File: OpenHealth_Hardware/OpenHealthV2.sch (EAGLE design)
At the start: 21 parts

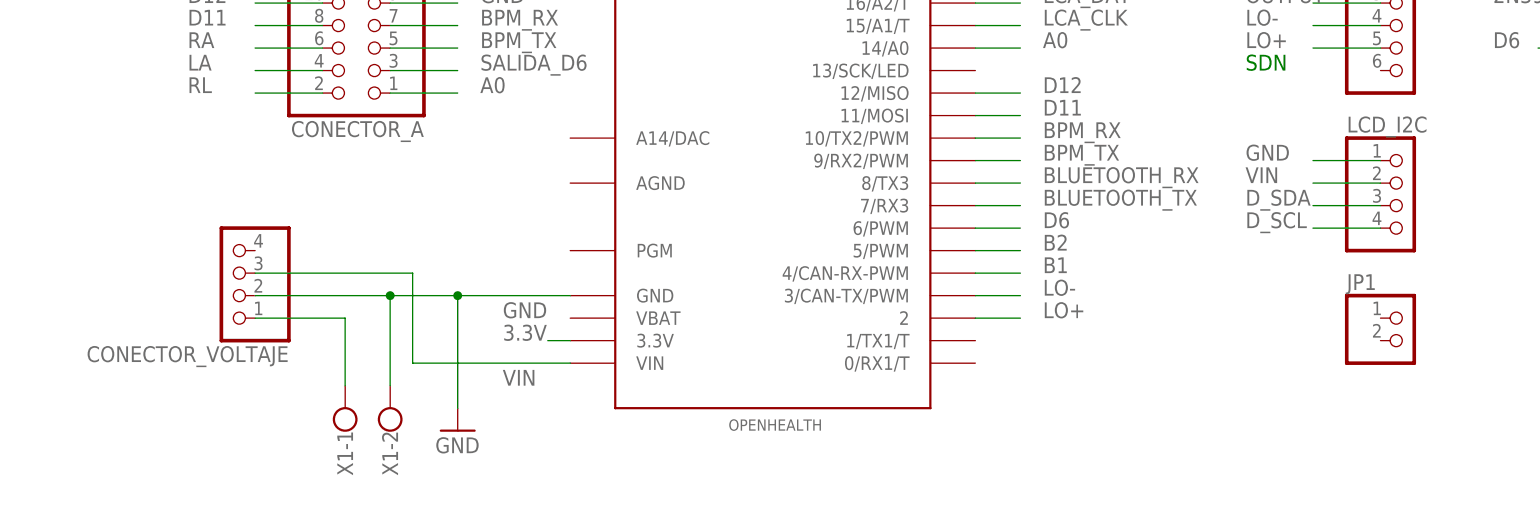
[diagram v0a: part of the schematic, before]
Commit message: Creacion de la Primera Libreria
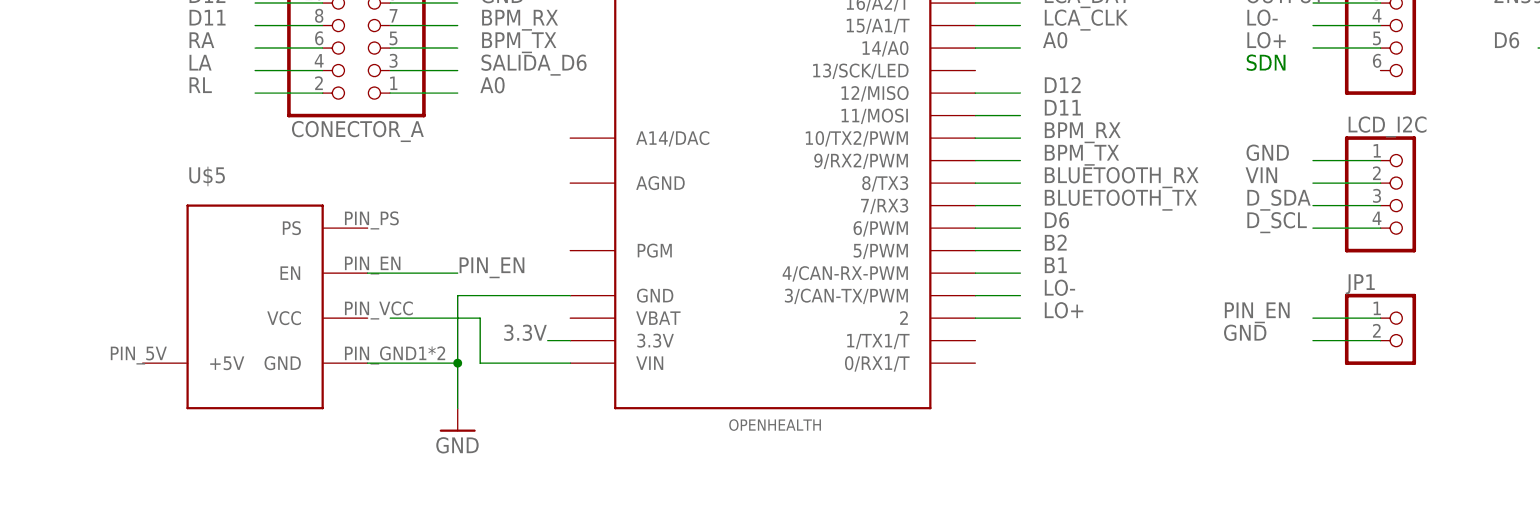
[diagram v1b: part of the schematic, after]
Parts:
- removed CONECTOR_VOLTAJE: (no value), pinhead:PINHD-1X4
- removed X1: (no value), con-wago-500:W237-102
- added U$5: LIPOWER, Bateria:LIPOWER
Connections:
- removed net N$1: CONECTOR_VOLTAJE.1, X1-1.KL
- new net N$5: OPENHEALTH.VIN
- new net PIN_EN: JP1.1, U$5.EN
- net GND: now also JP1.2, U$5.GND; no longer CONECTOR_VOLTAJE.2, X1-2.KL
- net VIN: no longer CONECTOR_VOLTAJE.3, OPENHEALTH.VIN
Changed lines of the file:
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@@
 <?xml version="1.0" encoding="utf-8"?>
 <!DOCTYPE eagle SYSTEM "eagle.dtd">
-<eagle version="7.2.0">
+<eagle version="7.7.0">
 <drawing>
 <settings>
@@
 <parts>
 <part name="OPENHEALTH" library="Teensy_3_and_LC_Series_Boards_v1.1" deviceset="TEENSY_3.1_OUTER_ROW" device=""/>
-<part name="CONECTOR_VOLTAJE" library="pinhead" deviceset="PINHD-1X4" device=""/>
-<part name="X1" library="con-wago-500" deviceset="W237-102" device=""/>
 <part name="CONECTOR_A" library="pinhead" deviceset="PINHD-2X5" device=""/>
 <part name="CONECTOR_B" library="pinhead" deviceset="PINHD-2X5" device=""/>
@@
 <part name="R4" library="resistor" deviceset="R-US_" device="0204/7" value="330"/>
 <part name="R5" library="resistor" deviceset="R-US_" device="0204/7" value="330"/>
+<part name="U$5" library="Bateria" deviceset="LIPOWER" device=""/>
 </parts>
 <sheets>
@@
 <instances>
 <instance part="OPENHEALTH" gate="G$1" x="-33.02" y="93.98" rot="R180"/>
-<instance part="CONECTOR_VOLTAJE" gate="A" x="-93.98" y="76.2" rot="R180"/>
-<instance part="X1" gate="-1" x="-81.28" y="58.42" rot="R90"/>
-<instance part="X1" gate="-2" x="-76.2" y="58.42" rot="R90"/>
 <instance part="CONECTOR_A" gate="A" x="-78.74" y="101.6" rot="R180"/>
 <instance part="CONECTOR_B" gate="A" x="-78.74" y="121.92" rot="R180"/>
@@
 <instance part="R4" gate="G$1" x="58.42" y="152.4" rot="R90"/>
 <instance part="R5" gate="G$1" x="66.04" y="152.4" rot="R90"/>
+<instance part="U$5" gate="G$1" x="-99.06" y="60.96"/>
 </instances>
 <busses>
 </busses>
 <nets>
-<net name="N$1" class="0">
-<segment>
-<pinref part="X1" gate="-1" pin="KL"/>
-<wire x1="-81.28" y1="71.12" x2="-81.28" y2="63.5" width="0.1524" layer="91"/>
-<pinref part="CONECTOR_VOLTAJE" gate="A" pin="1"/>
-<wire x1="-91.44" y1="71.12" x2="-81.28" y2="71.12" width="0.1524" layer="91"/>
-</segment>
-</net>
 <net name="GND" class="0">
-<segment>
-<pinref part="CONECTOR_VOLTAJE" gate="A" pin="2"/>
-<wire x1="-91.44" y1="73.66" x2="-76.2" y2="73.66" width="0.1524" layer="91"/>
-<pinref part="X1" gate="-2" pin="KL"/>
-<wire x1="-76.2" y1="73.66" x2="-68.58" y2="73.66" width="0.1524" layer="91"/>
-<wire x1="-68.58" y1="73.66" x2="-55.88" y2="73.66" width="0.1524" layer="91"/>
-<wire x1="-76.2" y1="63.5" x2="-76.2" y2="73.66" width="0.1524" layer="91"/>
-<junction x="-76.2" y="73.66"/>
-<pinref part="OPENHEALTH" gate="G$1" pin="GND"/>
-<label x="-63.5" y="71.12" size="1.778" layer="95"/>
-<pinref part="GND2" gate="1" pin="GND"/>
-<wire x1="-68.58" y1="60.96" x2="-68.58" y2="73.66" width="0.1524" layer="91"/>
-<junction x="-68.58" y="73.66"/>
-</segment>
 <segment>
 <pinref part="AD8232_A" gate="A" pin="1"/>
@@
 <label x="-66.04" y="121.92" size="1.778" layer="95"/>
 </segment>
+<segment>
+<pinref part="U$5" gate="G$1" pin="GND"/>
+<wire x1="-78.74" y1="66.04" x2="-68.58" y2="66.04" width="0.1524" layer="91"/>
+<wire x1="-68.58" y1="66.04" x2="-68.58" y2="73.66" width="0.1524" layer="91"/>
+<pinref part="OPENHEALTH" gate="G$1" pin="GND"/>
+<wire x1="-68.58" y1="73.66" x2="-55.88" y2="73.66" width="0.1524" layer="91"/>
+<pinref part="GND2" gate="1" pin="GND"/>
+<wire x1="-68.58" y1="66.04" x2="-68.58" y2="60.96" width="0.1524" layer="91"/>
+<junction x="-68.58" y="66.04"/>
+</segment>
+<segment>
+<pinref part="JP1" gate="G$1" pin="2"/>
+<wire x1="35.56" y1="68.58" x2="27.94" y2="68.58" width="0.1524" layer="91"/>
+<label x="17.78" y="68.58" size="1.778" layer="95"/>
+</segment>
 </net>
 <net name="VIN" class="0">
-<segment>
-<pinref part="CONECTOR_VOLTAJE" gate="A" pin="3"/>
-<wire x1="-91.44" y1="76.2" x2="-73.66" y2="76.2" width="0.1524" layer="91"/>
-<wire x1="-73.66" y1="76.2" x2="-73.66" y2="66.04" width="0.1524" layer="91"/>
-<pinref part="OPENHEALTH" gate="G$1" pin="VIN"/>
-<wire x1="-73.66" y1="66.04" x2="-55.88" y2="66.04" width="0.1524" layer="91"/>
-<label x="-63.5" y="63.5" size="1.778" layer="95"/>
-</segment>
 <segment>
 <pinref part="LCD_I2C" gate="A" pin="2"/>
@@
 </segment>
 </net>
+<net name="N$5" class="0">
+<segment>
+<wire x1="-76.2" y1="71.12" x2="-66.04" y2="71.12" width="0.1524" layer="91"/>
+<wire x1="-66.04" y1="71.12" x2="-66.04" y2="66.04" width="0.1524" layer="91"/>
+<pinref part="OPENHEALTH" gate="G$1" pin="VIN"/>
+<wire x1="-66.04" y1="66.04" x2="-55.88" y2="66.04" width="0.1524" layer="91"/>
+</segment>
+</net>
+<net name="PIN_EN" class="0">
+<segment>
+<pinref part="U$5" gate="G$1" pin="EN"/>
+<wire x1="-78.74" y1="76.2" x2="-68.58" y2="76.2" width="0.1524" layer="91"/>
+<label x="-68.58" y="76.2" size="1.778" layer="95"/>
+</segment>
+<segment>
+<pinref part="JP1" gate="G$1" pin="1"/>
+<wire x1="35.56" y1="71.12" x2="27.94" y2="71.12" width="0.1524" layer="91"/>
+<label x="17.78" y="71.12" size="1.778" layer="95"/>
+</segment>
+</net>

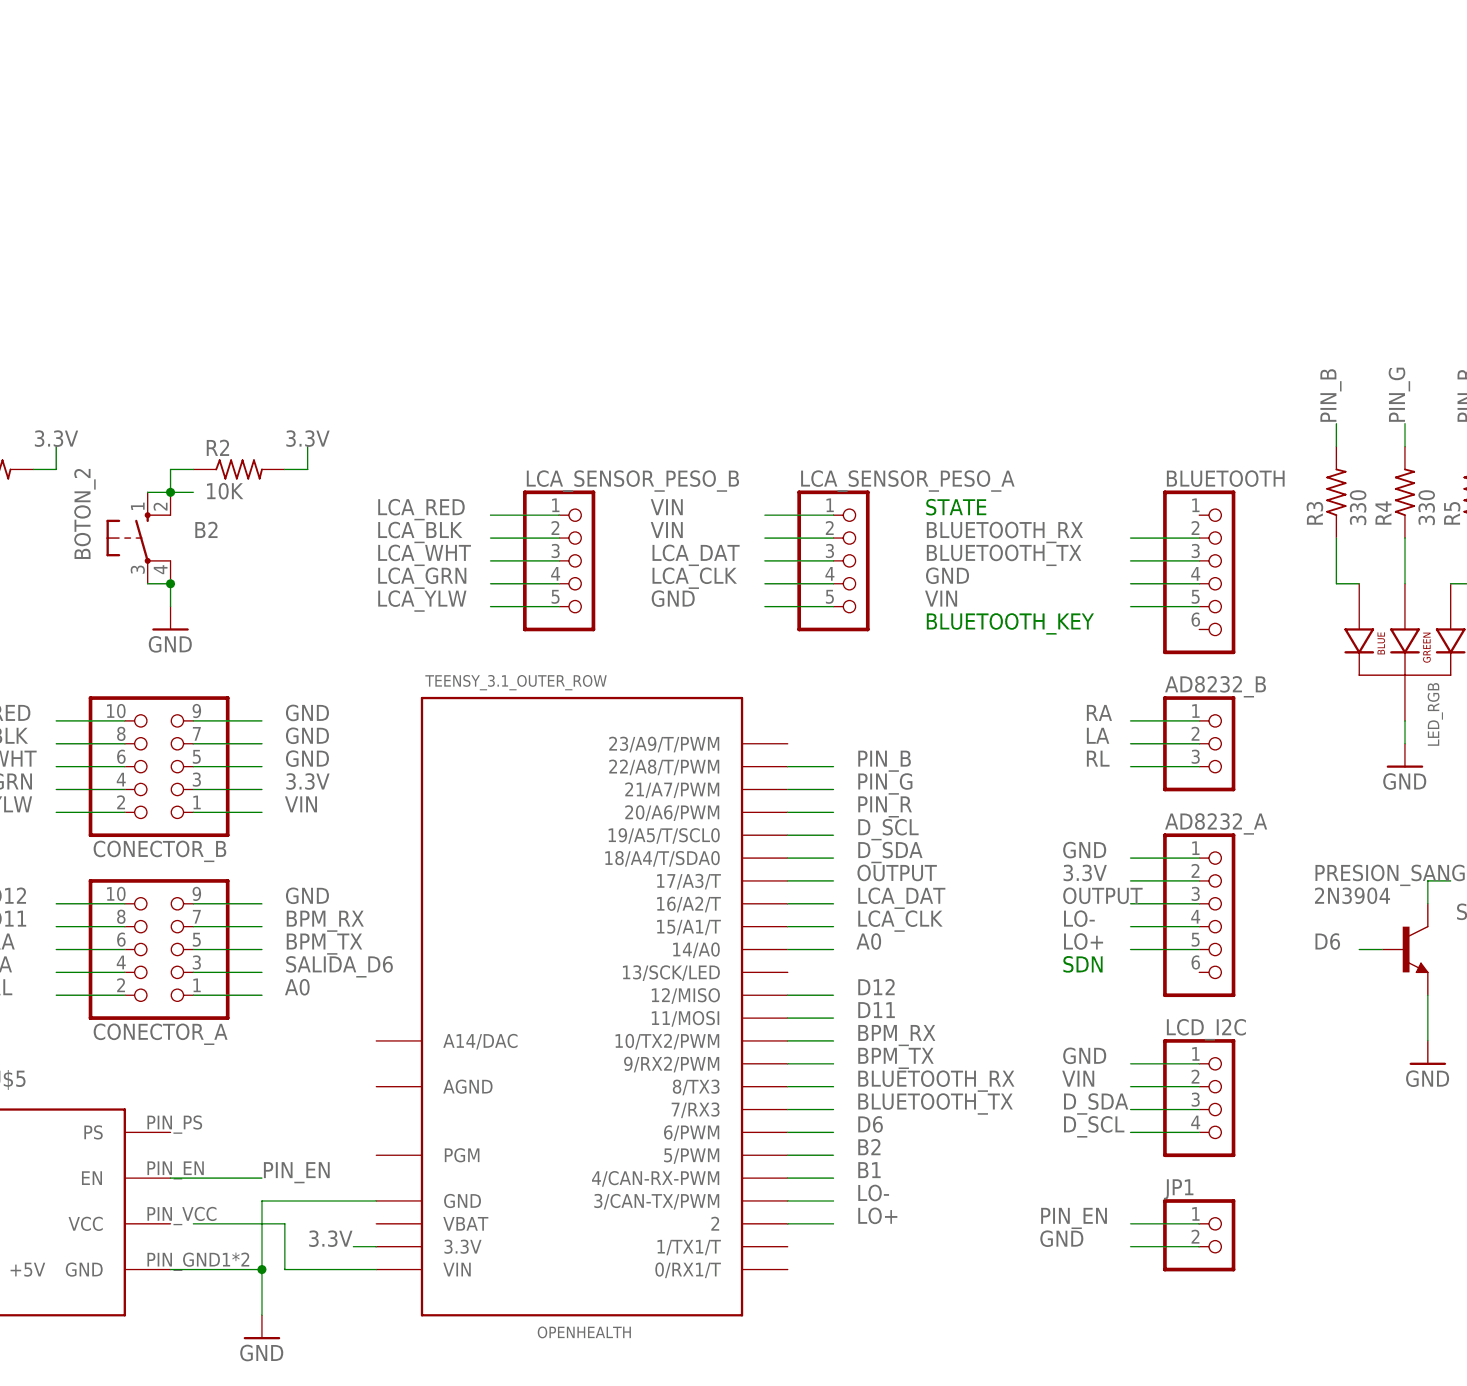
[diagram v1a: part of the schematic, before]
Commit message: Creacion de los modulos de bluetooth y ad8232 asi como el cambio de nombre de la libreria y la utilizacion de la libreria en el proyecto
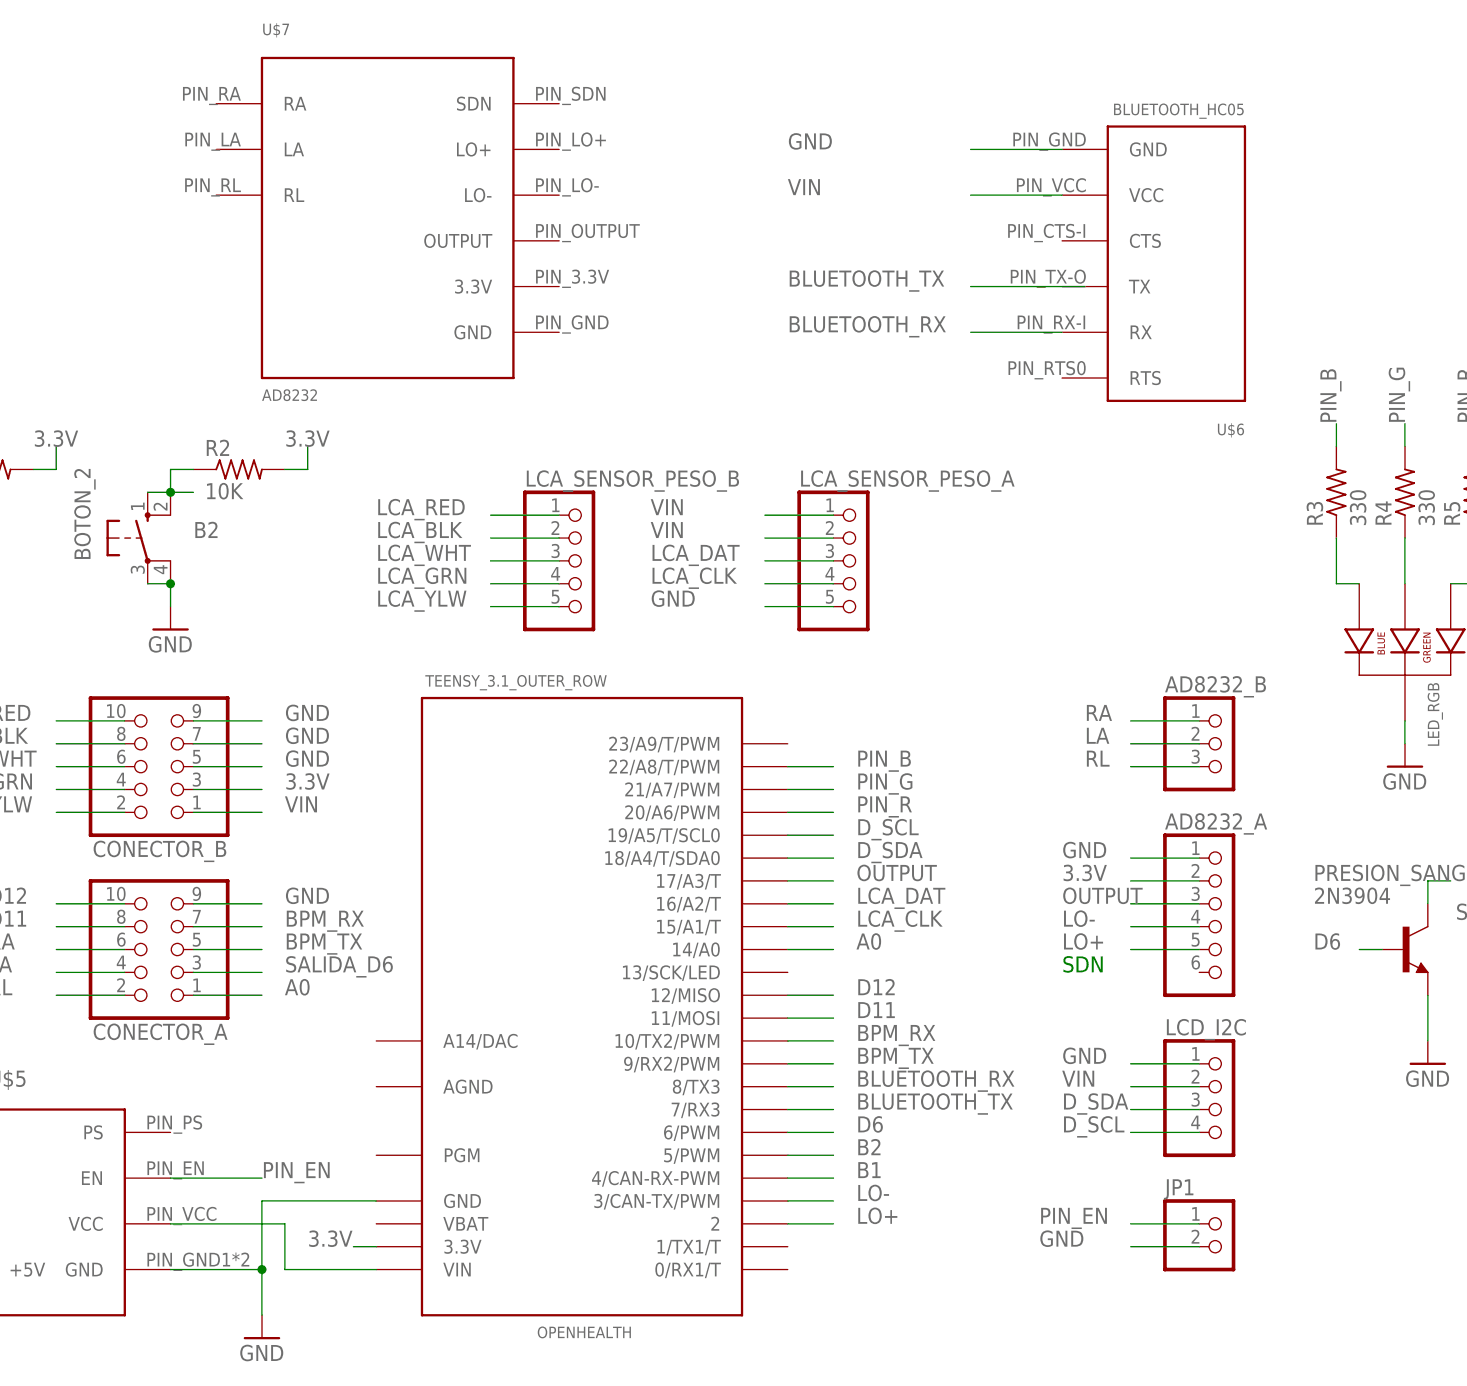
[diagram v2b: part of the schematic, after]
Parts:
- removed BLUETOOTH: (no value), pinhead:PINHD-1X6
- added U$6: BLUETOOTH_HC05, OpenHealth:BLUETOOTH_HC05
- added U$7: AD8232, OpenHealth:AD8232
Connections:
- net BLUETOOTH_RX: now also U$6.RX; no longer BLUETOOTH.2
- net BLUETOOTH_TX: no longer BLUETOOTH.3
- net GND: now also U$6.GND; no longer BLUETOOTH.4
- net N$5: now also U$5.VCC
- net VIN: now also U$6.VCC; no longer BLUETOOTH.5
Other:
- note removed: "BLUETOOTH_KEY"
- note removed: "STATE"
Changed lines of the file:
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@@
 <?xml version="1.0" encoding="utf-8"?>
 <!DOCTYPE eagle SYSTEM "eagle.dtd">
-<eagle version="7.7.0">
+<eagle version="7.2.0">
 <drawing>
 <settings>
@@
 <part name="GND3" library="supply1" deviceset="GND" device=""/>
 <part name="GND4" library="supply1" deviceset="GND" device=""/>
-<part name="BLUETOOTH" library="pinhead" deviceset="PINHD-1X6" device=""/>
 <part name="LCD_I2C" library="pinhead" deviceset="PINHD-1X4" device=""/>
 <part name="LCA_SENSOR_PESO_A" library="pinhead" deviceset="PINHD-1X5" device=""/>
@@
 <part name="R5" library="resistor" deviceset="R-US_" device="0204/7" value="330"/>
 <part name="U$5" library="Bateria" deviceset="LIPOWER" device=""/>
+<part name="U$6" library="OpenHealth" deviceset="BLUETOOTH_HC05" device=""/>
+<part name="U$7" library="OpenHealth" deviceset="AD8232" device=""/>
 </parts>
 <sheets>
 <sheet>
 <plain>
-<text x="5.08" y="137.16" size="1.778" layer="91">BLUETOOTH_KEY</text>
-<text x="5.08" y="149.86" size="1.778" layer="91">STATE</text>
 <text x="20.32" y="99.06" size="1.778" layer="91">SDN</text>
 </plain>
@@
 <instance part="GND3" gate="1" x="-78.74" y="137.16"/>
 <instance part="GND4" gate="1" x="-106.68" y="137.16"/>
-<instance part="BLUETOOTH" gate="A" x="38.1" y="142.24"/>
 <instance part="LCD_I2C" gate="A" x="38.1" y="83.82"/>
 <instance part="LCA_SENSOR_PESO_A" gate="A" x="-2.54" y="144.78"/>
@@
 <instance part="R5" gate="G$1" x="66.04" y="152.4" rot="R90"/>
 <instance part="U$5" gate="G$1" x="-99.06" y="60.96"/>
+<instance part="U$6" gate="G$1" x="40.64" y="193.04" rot="R180"/>
+<instance part="U$7" gate="G$1" x="-68.58" y="165.1"/>
 </instances>
 <busses>
@@
 <pinref part="LED_RGB" gate="G$1" pin="CATHODE"/>
 <wire x1="58.42" y1="124.46" x2="58.42" y2="127" width="0.1524" layer="91"/>
-</segment>
-<segment>
-<pinref part="BLUETOOTH" gate="A" pin="4"/>
-<wire x1="35.56" y1="142.24" x2="27.94" y2="142.24" width="0.1524" layer="91"/>
-<label x="5.08" y="142.24" size="1.778" layer="95"/>
 </segment>
 <segment>
@@
 <label x="17.78" y="68.58" size="1.778" layer="95"/>
 </segment>
+<segment>
+<pinref part="U$6" gate="G$1" pin="GND"/>
+<wire x1="20.32" y1="190.5" x2="10.16" y2="190.5" width="0.1524" layer="91"/>
+<label x="-10.16" y="190.5" size="1.778" layer="95"/>
+</segment>
 </net>
 <net name="VIN" class="0">
@@
 </segment>
 <segment>
-<pinref part="BLUETOOTH" gate="A" pin="5"/>
-<wire x1="35.56" y1="139.7" x2="27.94" y2="139.7" width="0.1524" layer="91"/>
-<label x="5.08" y="139.7" size="1.778" layer="95"/>
-</segment>
-<segment>
 <pinref part="LCA_SENSOR_PESO_A" gate="A" pin="1"/>
 <wire x1="-12.7" y1="149.86" x2="-5.08" y2="149.86" width="0.1524" layer="91"/>
@@
 <wire x1="-76.2" y1="116.84" x2="-68.58" y2="116.84" width="0.1524" layer="91"/>
 <label x="-66.04" y="116.84" size="1.778" layer="95"/>
+</segment>
+<segment>
+<pinref part="U$6" gate="G$1" pin="VCC"/>
+<wire x1="20.32" y1="185.42" x2="10.16" y2="185.42" width="0.1524" layer="91"/>
+<label x="-10.16" y="185.42" size="1.778" layer="95"/>
 </segment>
 </net>
@@
 <net name="BLUETOOTH_RX" class="0">
 <segment>
-<pinref part="BLUETOOTH" gate="A" pin="2"/>
-<wire x1="35.56" y1="147.32" x2="27.94" y2="147.32" width="0.1524" layer="91"/>
-<label x="5.08" y="147.32" size="1.778" layer="95"/>
-</segment>
-<segment>
 <pinref part="OPENHEALTH" gate="G$1" pin="8/TX3"/>
 <wire x1="-10.16" y1="86.36" x2="-5.08" y2="86.36" width="0.1524" layer="91"/>
 <label x="-2.54" y="86.36" size="1.778" layer="95"/>
 </segment>
+<segment>
+<pinref part="U$6" gate="G$1" pin="RX"/>
+<wire x1="20.32" y1="170.18" x2="10.16" y2="170.18" width="0.1524" layer="91"/>
+<label x="-10.16" y="170.18" size="1.778" layer="95"/>
+</segment>
 </net>
 <net name="BLUETOOTH_TX" class="0">
-<segment>
-<pinref part="BLUETOOTH" gate="A" pin="3"/>
-<wire x1="35.56" y1="144.78" x2="27.94" y2="144.78" width="0.1524" layer="91"/>
-<label x="5.08" y="144.78" size="1.778" layer="95"/>
-</segment>
 <segment>
 <pinref part="OPENHEALTH" gate="G$1" pin="7/RX3"/>
 <wire x1="-10.16" y1="83.82" x2="-5.08" y2="83.82" width="0.1524" layer="91"/>
 <label x="-2.54" y="83.82" size="1.778" layer="95"/>
+</segment>
+<segment>
+<wire x1="22.86" y1="175.26" x2="10.16" y2="175.26" width="0.1524" layer="91"/>
+<label x="-10.16" y="175.26" size="1.778" layer="95"/>
 </segment>
 </net>
@@
 <net name="N$5" class="0">
 <segment>
-<wire x1="-76.2" y1="71.12" x2="-66.04" y2="71.12" width="0.1524" layer="91"/>
+<wire x1="-78.74" y1="71.12" x2="-66.04" y2="71.12" width="0.1524" layer="91"/>
 <wire x1="-66.04" y1="71.12" x2="-66.04" y2="66.04" width="0.1524" layer="91"/>
 <pinref part="OPENHEALTH" gate="G$1" pin="VIN"/>
 <wire x1="-66.04" y1="66.04" x2="-55.88" y2="66.04" width="0.1524" layer="91"/>
-</segment>
-</net>
+<pinref part="U$5" gate="G$1" pin="VCC"/>
+</segment>
+</net>
